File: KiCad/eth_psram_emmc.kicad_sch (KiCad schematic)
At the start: 43 parts, among them IC6 LAN8742A-CZ-TR, IC7 APS256XXN-OBR-BG, X4 5033981892, Y2 VXM7-9032-25M0000000

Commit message: #22
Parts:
- added JP3: (no value), PCM_EEZ_SMD:JP2 open (0603), symbol PCM_EEZ_unsorted:JP2 open
- added JP4: (no value), PCM_EEZ_SMD:JP3 shorted (0603), symbol PCM_EEZ_unsorted:JP3 shorted
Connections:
- net +3V3: now also JP4.NC; no longer R12.2
- net GND: now also JP4.NO
- net at C44.2, IC6.5 (XTAL1/CLKIN), Y2.3: now also JP3.2
- new net: JP4.COM, R12.2
- new net ETH_CLK: JP3.1
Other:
- moved on the sheet: C43, C44, C46, C47, C48, C49, C50, C51, C52, C53, FB2, IC6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

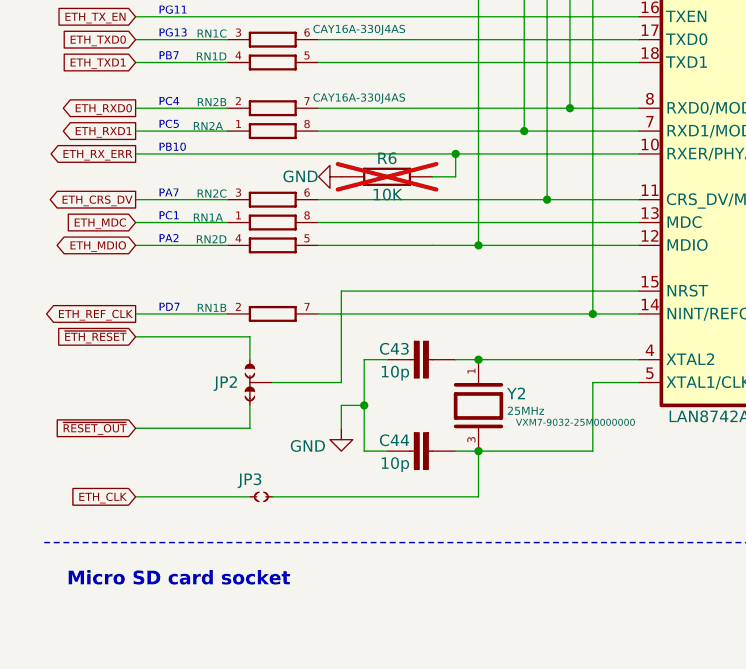
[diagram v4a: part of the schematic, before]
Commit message: Ethernet PHY no xtal variant added
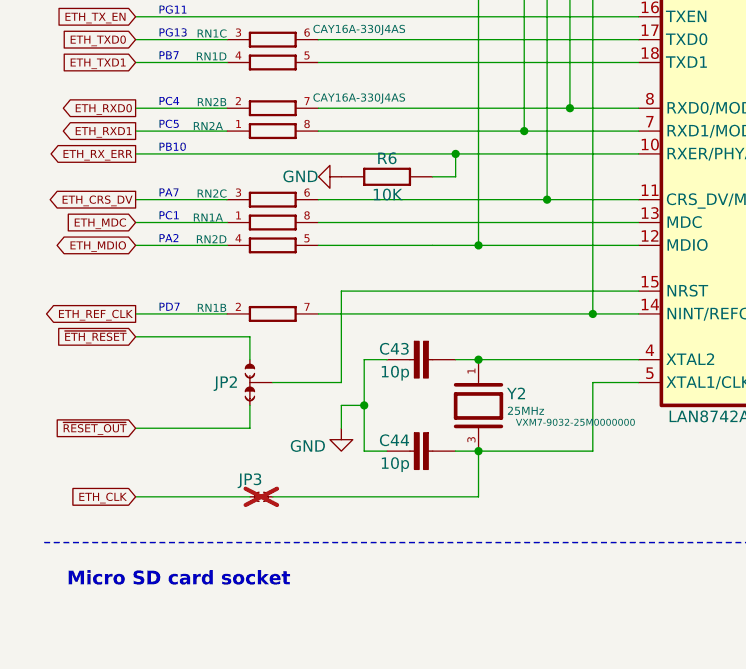
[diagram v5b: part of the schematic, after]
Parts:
- JP3: footprint PCM_EEZ_SMD:JP2 open (0603) -> PCM_EEZ_SMD:JP2 open (0402); now not fitted
- R6: now fitted; now in the parts list
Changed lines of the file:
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@@
 	(title_block
 		(title "${project_name}")
-		(date "2026-04-20")
+		(date "2026-04-21")
 		(rev "${project_version}")
 		(company "${project_creator}")
@@
 		(on_board yes)
 		(in_pos_files yes)
-		(dnp no)
+		(dnp yes)
 		(property "Reference" "JP3"
 			(at 36.83 86.995 0)
@@
 		)
 		(property "Value" ""
-			(at 38.1 88.9 0)
-			(hide yes)
+			(at 38.735 90.805 0)
 			(show_name no)
 			(do_not_autoplace no)
@@
 			)
 		)
-		(property "Footprint" "PCM_EEZ_SMD:JP2 open (0603)"
+		(property "Footprint" "PCM_EEZ_SMD:JP2 open (0402)"
 			(at 38.1 91.44 0)
 			(hide yes)
@@
 			)
 		)
+		(property "DigiKey" ""
+			(at 38.1 88.9 0)
+			(hide yes)
+			(show_name no)
+			(do_not_autoplace no)
+			(effects
+				(font
+					(size 0.889 0.889)
+				)
+			)
+		)
+		(property "Mouser" ""
+			(at 38.1 88.9 0)
+			(hide yes)
+			(show_name no)
+			(do_not_autoplace no)
+			(effects
+				(font
+					(size 0.889 0.889)
+				)
+			)
+		)
+		(property "TME" ""
+			(at 38.1 88.9 0)
+			(hide yes)
+			(show_name no)
+			(do_not_autoplace no)
+			(effects
+				(font
+					(size 0.889 0.889)
+				)
+			)
+		)
+		(property "LCSC" ""
+			(at 38.1 88.9 0)
+			(hide yes)
+			(show_name no)
+			(do_not_autoplace no)
+			(effects
+				(font
+					(size 0.889 0.889)
+				)
+			)
+		)
 		(pin "1"
 		)
@@
 					(reference "JP3")
 					(unit 1)
+					(variant
+						(name "Ethernet PHY no xtal")
+						(dnp no)
+						(in_bom yes)
+						(field
+							(name "DigiKey")
+							(value "13-RC0402FR-1349R9LCT-ND")
+						)
+						(field
+							(name "LCSC")
+							(value "C4007649")
+						)
+						(field
+							(name "Mouser")
+							(value "603-RC0402FR-1349R9L")
+						)
+						(field
+							(name "TME")
+							(value "RC0402FR-0749R9L")
+						)
+						(field
+							(name "Value")
+							(value "49R9")
+						)
+					)
 				)
 			)
@@
 					(reference "Y2")
 					(unit 1)
+					(variant
+						(name "Ethernet PHY no xtal")
+						(dnp yes)
+						(in_bom no)
+					)
 				)
 			)
@@
 		(body_style 1)
 		(exclude_from_sim no)
-		(in_bom no)
+		(in_bom yes)
 		(on_board yes)
 		(in_pos_files yes)
-		(dnp yes)
+		(dnp no)
 		(property "Reference" "R6"
 			(at 53.34 52.07 90)
@@
 					(reference "R6")
 					(unit 1)
+					(variant
+						(name "Ethernet PHY no xtal")
+						(dnp yes)
+						(in_bom no)
+					)
 				)
 			)
@@
 					(reference "C43")
 					(unit 1)
+					(variant
+						(name "Ethernet PHY no xtal")
+						(dnp yes)
+						(in_bom no)
+					)
 				)
 			)
@@
 					(reference "C44")
 					(unit 1)
+					(variant
+						(name "Ethernet PHY no xtal")
+						(dnp yes)
+						(in_bom no)
+					)
 				)
 			)
